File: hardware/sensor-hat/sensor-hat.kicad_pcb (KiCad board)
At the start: 2 copper layers, 120 x 49 mm, 60 parts, among them J1 1x20 socket, bottom, J10 EZO socket, top, J11 EZO socket, top, J12 EZO socket, top, J13 EZO socket, top, J14 EZO socket, top, J16 DNP, J2 1x20 socket, bottom, J3 pH probe, J4 ORP probe, J5 EZO probe, J6 1-Wire, J7 contacts, J8 4-20 mA, J9 EZO socket, top

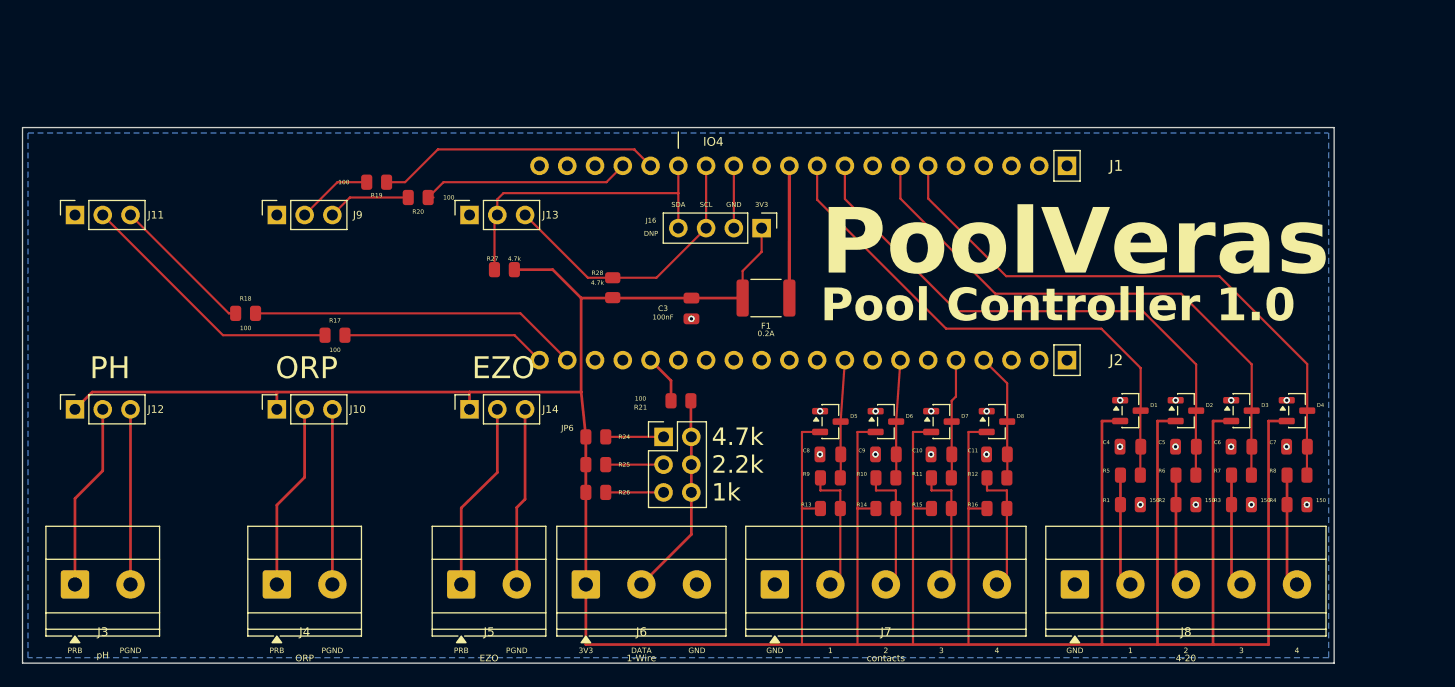
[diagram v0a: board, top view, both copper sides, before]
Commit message: Lay out the PoolVeras V1.1 hat with the display, Atlas boards, and two buttons.
Socket 3 stays on the display I2C bus, and the screen shows pH, ORP, and water temperature.

Co-authored-by: Cursor <cursoragent@cursor.com>
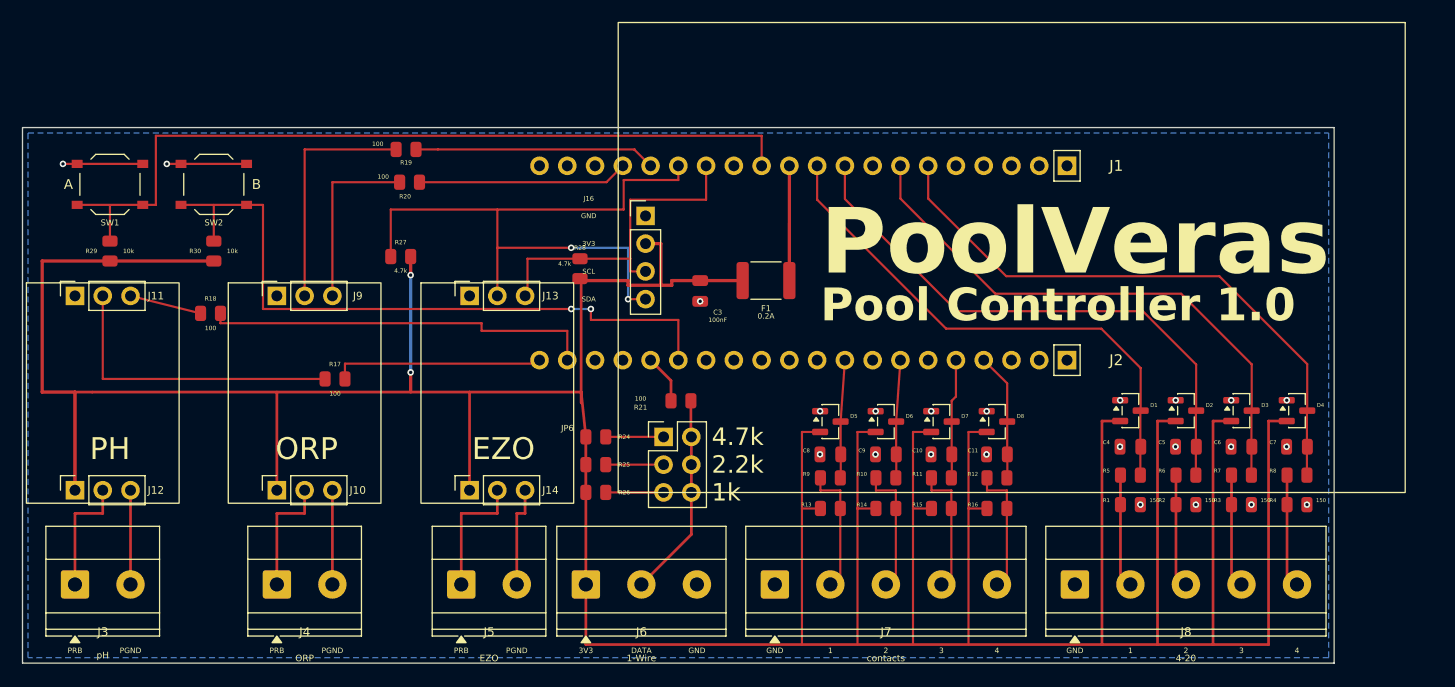
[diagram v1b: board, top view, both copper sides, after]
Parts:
- added DISP1: SSD1309, SensorHat:SSD1309, F.Cu at (57.0, 8.08)
- added EZO1: pH, SensorHat:Atlas_EZO, F.Cu at (7.34, 24.3)
- added EZO2: ORP, SensorHat:Atlas_EZO, F.Cu at (25.8, 24.3)
- added EZO3: EZO, SensorHat:Atlas_EZO, F.Cu at (43.4, 24.3)
- added R29: 10k, PCM_JLCPCB:R_0805, F.Cu at (8.00, 11.3)
- added R30: 10k, PCM_JLCPCB:R_0805, F.Cu at (17.5, 11.3)
- added SW1: push, Button_Switch_SMD:SW_Push_1P1T_XKB_TS-1187A, F.Cu at (8.00, 5.20)
- added SW2: push, Button_Switch_SMD:SW_Push_1P1T_XKB_TS-1187A, F.Cu at (17.5, 5.20)
- J16: value DNP -> Socket; footprint Connector_PinHeader_2.54mm:PinHeader_1x04_P2.54mm_Vertical -> Connector_PinSocket_2.54mm:PinSocket_1x04_P2.54mm_Vertical
- moved J16 10.7 mm to (57.0, 8.08), turned to 0 degrees
- moved R27 9.57 mm to (34.6, 11.8)
- moved J11 7.40 mm to (4.80, 15.4)
- moved J13 7.40 mm to (40.9, 15.4)
- moved J9 7.40 mm to (23.3, 15.4)
- moved J10 7.40 mm to (23.3, 33.2)
- moved J12 7.40 mm to (4.80, 33.2)
- moved J14 7.40 mm to (40.9, 33.2)
- moved R19 4.03 mm to (35.1, 2.00)
- moved R17 4.00 mm to (28.6, 23.0)
- moved R28 3.47 mm to (51.0, 12.9)
- moved R18 3.21 mm to (17.2, 17.0)
- moved C3 1.79 mm to (62.0, 14.9)
- moved R20 1.61 mm to (35.4, 5.00)
- moved F1 1.60 mm to (68.0, 14.0)
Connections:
- J1 pad 12: (no net) -> BTN1
- J16 pad 1: V3OUT -> GND
- J16 pad 2: GND -> V3OUT
- J2 pad 15: (no net) -> BTN2
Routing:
- net BTN1: track 0.00 -> 75.0 mm
- net V3OUT: track 358.1 -> 427.9 mm, vias 0 -> 2
- net BTN2: track 0.00 -> 63.0 mm, vias 0 -> 2
- net SDA: track 29.7 -> 60.8 mm, vias 0 -> 2
- net EZO_ORP_TX: track 6.92 -> 21.8 mm
- net EZO_ORP_RX: track 7.60 -> 16.5 mm
- net GND: track 5.70 -> 14.6 mm, vias 22 -> 24
- net PH_PGND: track 16.0 -> 8.62 mm
- net ORP_PGND: track 16.0 -> 8.62 mm
- net EZO_PGND: track 16.3 -> 9.38 mm
- net EZO_PH_RX: track 13.3 -> 6.61 mm
- net PH_PRB: track 17.1 -> 11.2 mm
- net ORP_PRB: track 17.1 -> 11.2 mm
- net EPH_TX: track 30.3 -> 36.0 mm
- net EZO_PRB: track 17.4 -> 11.9 mm
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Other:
- board text added: "A"
- board text added: "B"
- board text removed: "DNP"
- board text removed: "IO4"

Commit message: Record the hat after the display, button, and routing passes.
The board now keeps the packed Atlas modules, the external switch header, and the shorter front-side wiring.

Co-authored-by: Cursor <cursoragent@cursor.com>
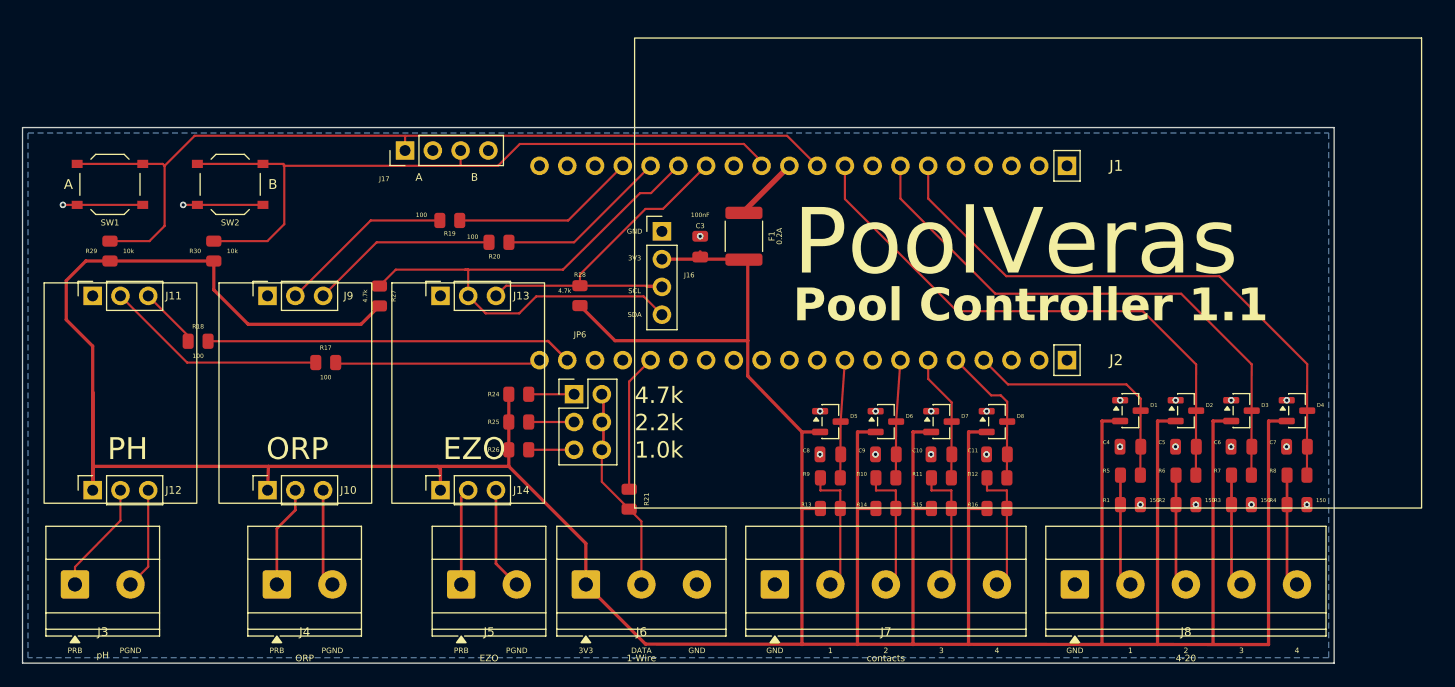
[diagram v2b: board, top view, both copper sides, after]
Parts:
- added J17: external, Connector_PinHeader_2.54mm:PinHeader_1x04_P2.54mm_Vertical, F.Cu at (35.0, 2.10)
- moved R21 10.2 mm to (55.5, 34.0), turned to 90 degrees
- moved R20 9.86 mm to (43.6, 10.5)
- moved JP6 9.07 mm to (50.5, 24.4)
- moved R24 8.06 mm to (45.4, 24.4)
- moved R26 8.06 mm to (45.4, 29.5)
- moved R25 8.06 mm to (45.4, 26.9)
- moved R19 7.63 mm to (39.1, 8.50)
- moved F1 4.53 mm to (66.0, 9.95), turned to -90 degrees
- moved R27 4.10 mm to (32.6, 15.4), turned to 90 degrees
- moved C3 4.05 mm to (62.0, 10.9), turned to 90 degrees
- moved R18 2.79 mm to (16.1, 19.6)
- moved EZO3 2.66 mm to (40.8, 24.3)
- moved J13 2.66 mm to (38.2, 15.4)
- moved J14 2.66 mm to (38.2, 33.2)
- moved R28 2.47 mm to (51.0, 15.4)
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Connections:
- J1 pad 10: ADC1 -> BTN1
- J1 pad 12: BTN1 -> BTN2
- J1 pad 16: EOR_RX -> EOR_TX
- J1 pad 17: EOR_TX -> EOR_RX
- J2 pad 15: BTN2 -> (no net)
- J2 pad 4: DIN4 -> ADC1
- J2 pad 5: DIN3 -> DIN4
- J2 pad 6: (no net) -> DIN3
- SW1 pad 1: GND -> BTN1
- SW1 pad 2: BTN1 -> GND
- SW2 pad 1: GND -> BTN2
- SW2 pad 2: BTN2 -> GND
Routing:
- net ADC1: track 48.9 -> 22.9 mm
- net OWGPIO: track 4.49 -> 12.6 mm
- net EZO_PH_TX: track 27.9 -> 20.4 mm
- net BTN1: track 75.0 -> 82.5 mm
- net SDA: track 60.8 -> 54.3 mm, vias 2 -> 0
- net V3OUT: track 427.9 -> 422.0 mm, vias 2 -> 0
- net EZO_ORP_TX: track 21.8 -> 16.3 mm
- net EOR_RX: track 22.1 -> 17.0 mm
- net BTN2: track 63.0 -> 67.5 mm, vias 2 -> 0
- net EOR_TX: track 19.2 -> 15.9 mm
- net EZO_PRB: track 11.9 -> 8.88 mm
- net SCL: track 31.0 -> 33.9 mm
- net +3V3: track 10.5 -> 8.26 mm
- net ORP_PRB: track 11.2 -> 9.32 mm
- net DIN4: track 11.7 -> 13.2 mm
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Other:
- board text added: "1.0k"
- board text added: "Pool Controller 1.1"
- board text removed: "1k"
- board text removed: "Pool Controller 1.0"

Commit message: Match the controller to the finished hat pinout and the 1-Wire slide switch.
Co-authored-by: Cursor <cursoragent@cursor.com>
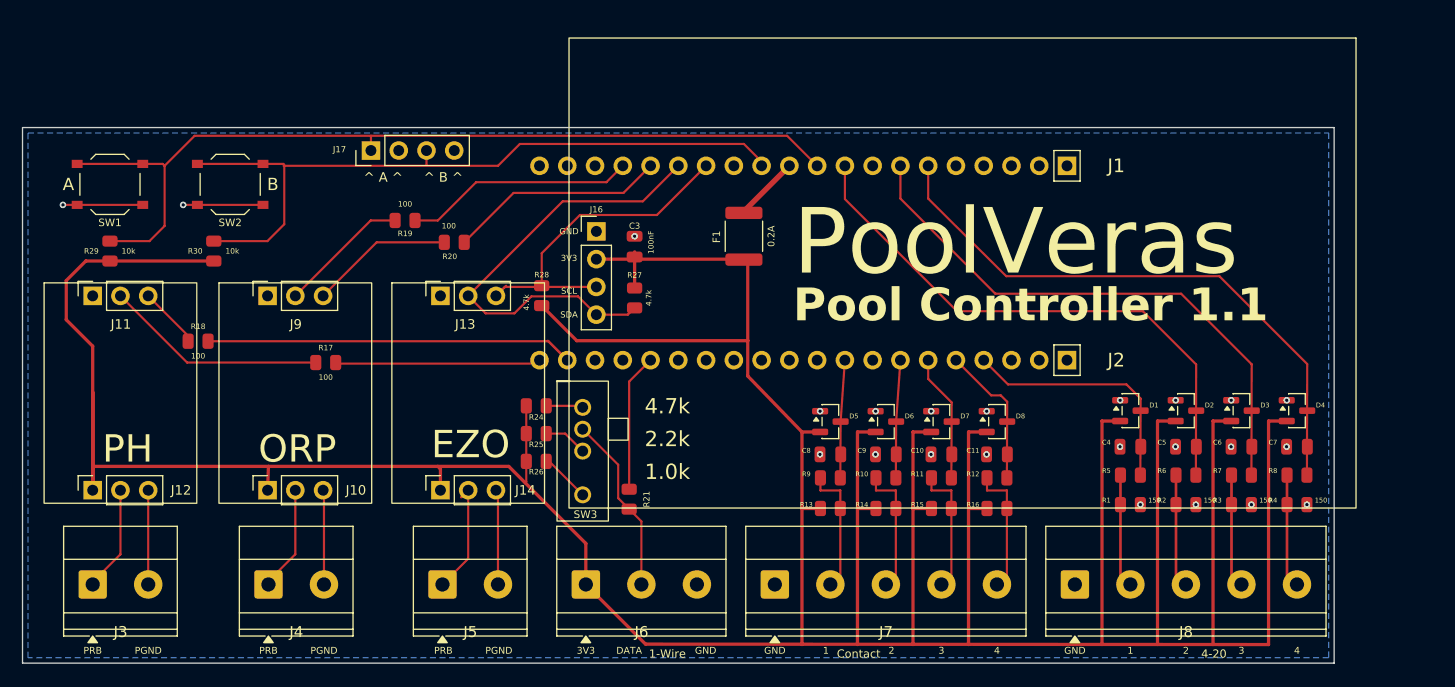
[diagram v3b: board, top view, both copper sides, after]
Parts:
- removed JP6: one shunt, Connector_PinHeader_2.54mm:PinHeader_2x03_P2.54mm_Vertical
- added SW3: SK13D07VG5, SensorHat:SW_SK13D07VG5, F.Cu at (51.2, 25.6)
- moved R27 23.4 mm to (56.0, 15.6), turned to -90 degrees
- moved C3 6.00 mm to (56.0, 10.9)
- moved DISP1 6.00 mm to (52.5, 9.50)
- moved J16 6.00 mm to (52.5, 9.50)
- moved R19 4.09 mm to (35.0, 8.50)
- moved R20 4.09 mm to (39.5, 10.5)
- moved R28 3.50 mm to (47.5, 15.4)
- moved J17 3.12 mm to (31.9, 2.10)
- moved R24 1.92 mm to (47.0, 25.5)
- moved R25 1.92 mm to (47.0, 28.0)
- moved R26 1.92 mm to (47.0, 30.5)
- moved J5 1.72 mm to (38.4, 41.8)
- moved J3 1.62 mm to (6.42, 41.8)
- moved J4 0.77 mm to (22.5, 41.8)
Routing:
- net SDA: track 54.3 -> 41.6 mm
- net V3OUT: track 422.0 -> 415.1 mm
- net EOR_RX: track 17.0 -> 21.1 mm
- net EOR_TX: track 15.9 -> 19.9 mm
- net EZO_ORP_TX: track 16.3 -> 12.2 mm
- net EZO_ORP_RX: track 17.2 -> 13.1 mm
- net OW: track 19.2 -> 16.6 mm
- net EZO_PRB: track 8.88 -> 10.5 mm
- net PU47: track 4.30 -> 3.40 mm
- net SCL: track 33.9 -> 33.0 mm
- net EZO_PGND: track 9.41 -> 8.70 mm
- net PH_PGND: track 9.29 -> 8.62 mm
- net PH_PRB: track 10.3 -> 9.67 mm
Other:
- board text added: "Contact"
- board text added: "^ A ^"
- board text added: "^ B ^"
- board text removed: "contacts"
- board text removed: "pH"
